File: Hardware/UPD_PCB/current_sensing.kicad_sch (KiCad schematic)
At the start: 68 parts, among them IC1 STS30-DIS, Q7 BSS84, U1 ACS711xEXLT-31AB, U2 INA219AxD, U3 INA219AxD, U4 INA219AxD, U5 INA219AxD, U6 INA219AxD, U7 INA219AxD

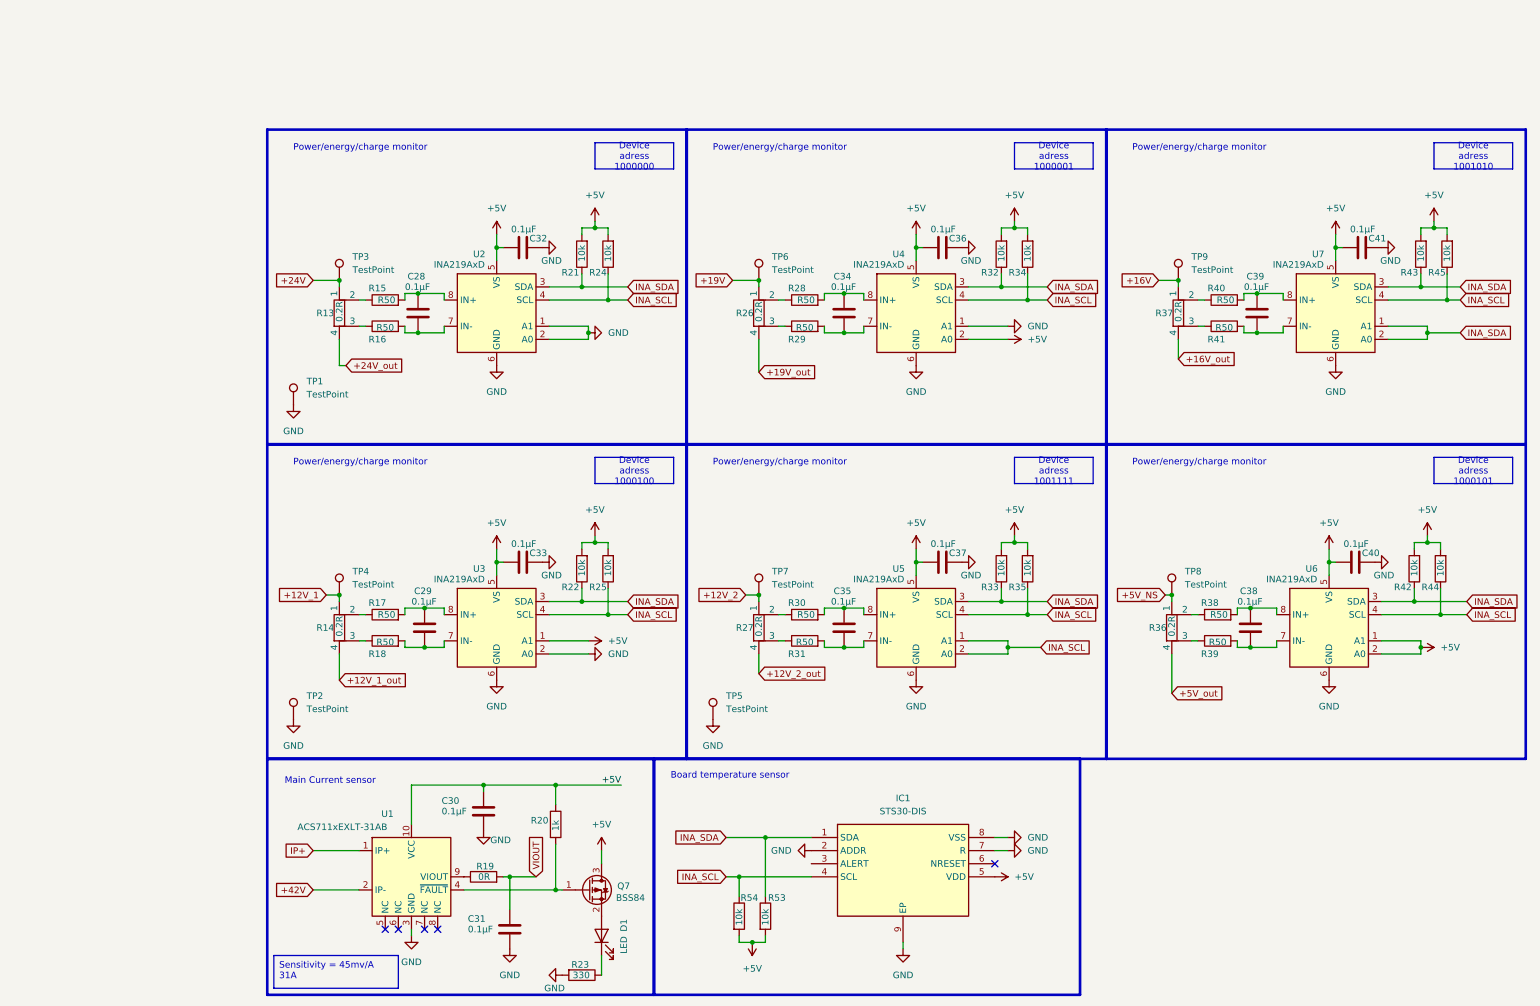
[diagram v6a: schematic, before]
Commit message: Routed main traces
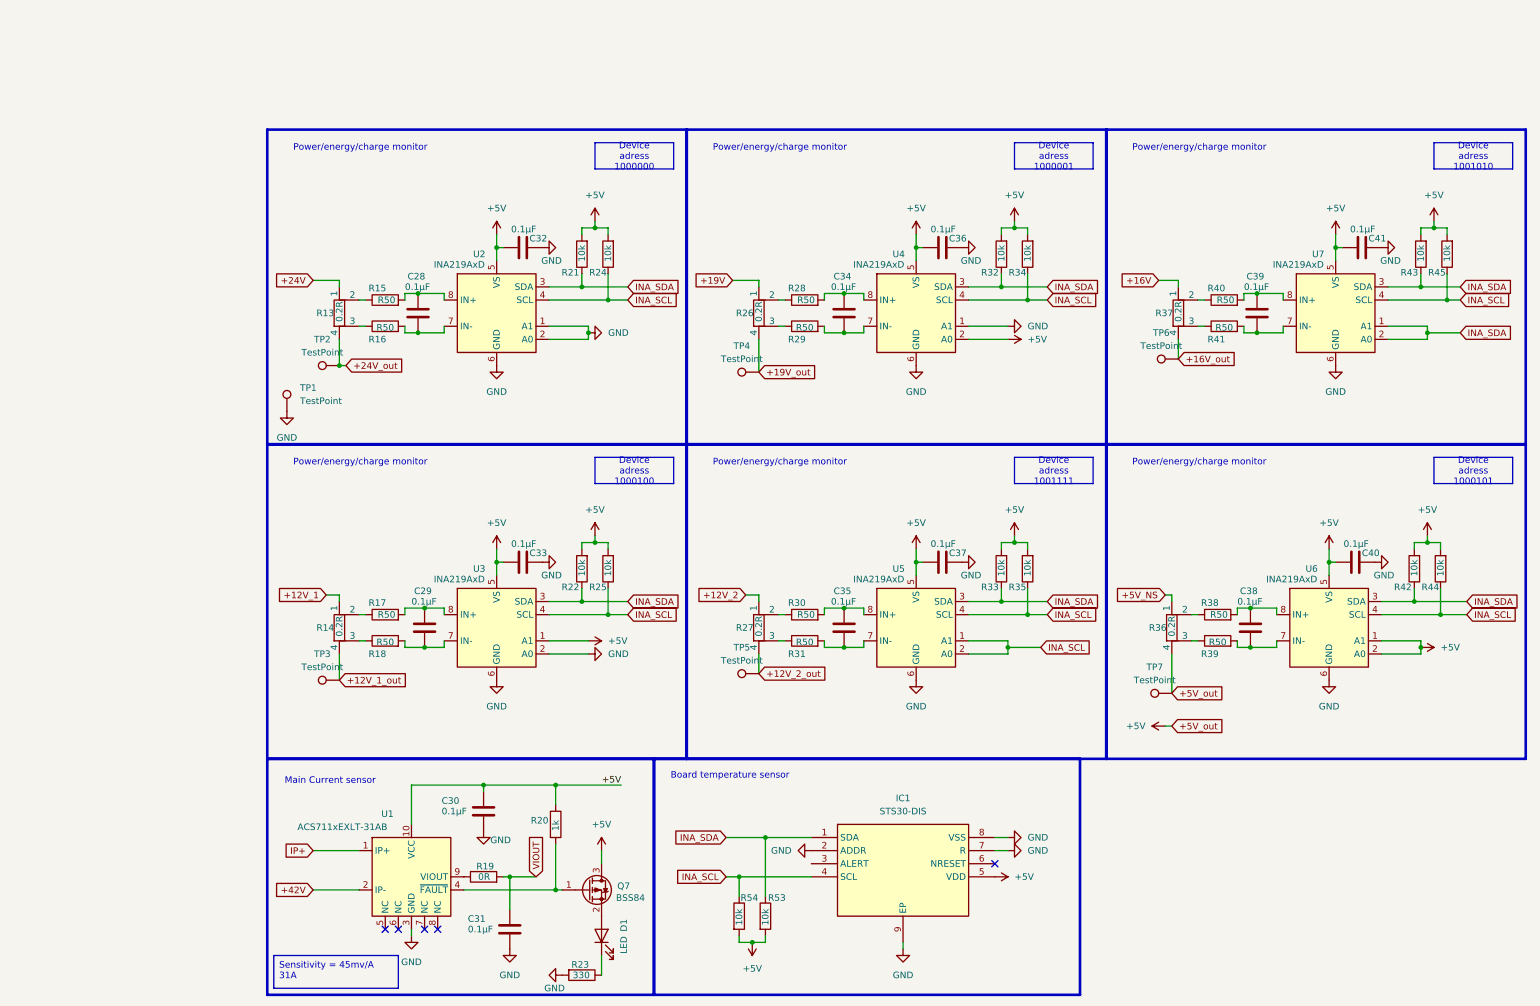
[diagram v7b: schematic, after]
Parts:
- removed TP8, TP9: TestPoint, TestPoint:TestPoint_THTPad_D1.0mm_Drill0.5mm, symbol Connector:TestPoint
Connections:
- net +5V_out is gone; now on net +5V: R36.4
- net +12V_1: no longer TP4.1
- net +12V_1_out: now also TP3.1
- net +12V_2: no longer TP7.1
- net +12V_2_out: now also TP5.1
- net +16V_out: now also TP6.1
- net +19V: no longer TP6.1
- net +19V_out: now also TP4.1
- net +24V: no longer TP3.1
- net +24V_out: now also TP2.1
- net +5V: now also TP7.1
- net GND: no longer TP2.1, TP5.1
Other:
- moved on the sheet: TP1

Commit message: Finalized pcb
Connector still needs to be changed
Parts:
- R14: value 0.2R -> 2mR
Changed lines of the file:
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@@
 			)
 		)
-		(property "Value" "0.2R"
+		(property "Value" "2mR"
 			(at 81.28 138.684 90)
 			(effects
